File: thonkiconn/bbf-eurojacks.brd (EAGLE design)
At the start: 18.4 x 52.1 mm, 7 parts, among them U1 THONKICONNNEW, U2 THONKICONNNEW, U3 THONKI-STEREO, U4 THONKI-STEREO

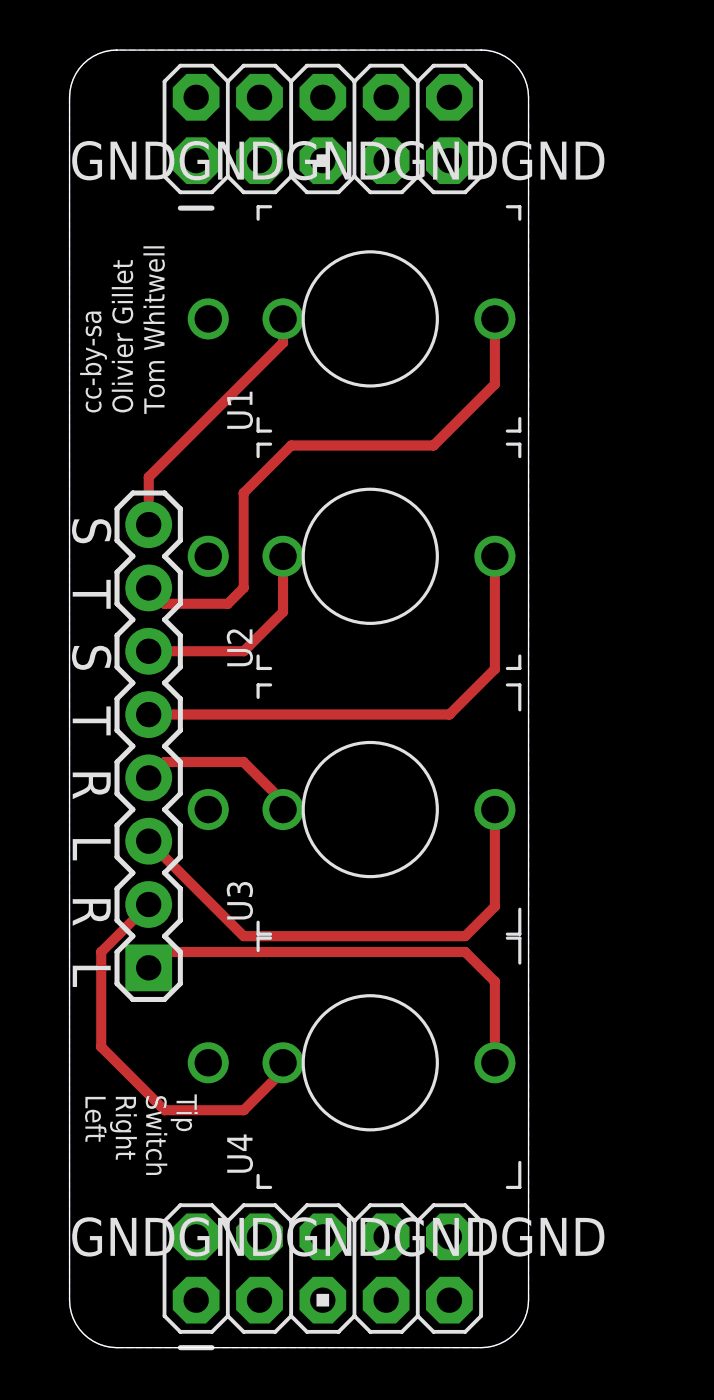
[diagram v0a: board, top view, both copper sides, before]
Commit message: Finished updated eurojacks board
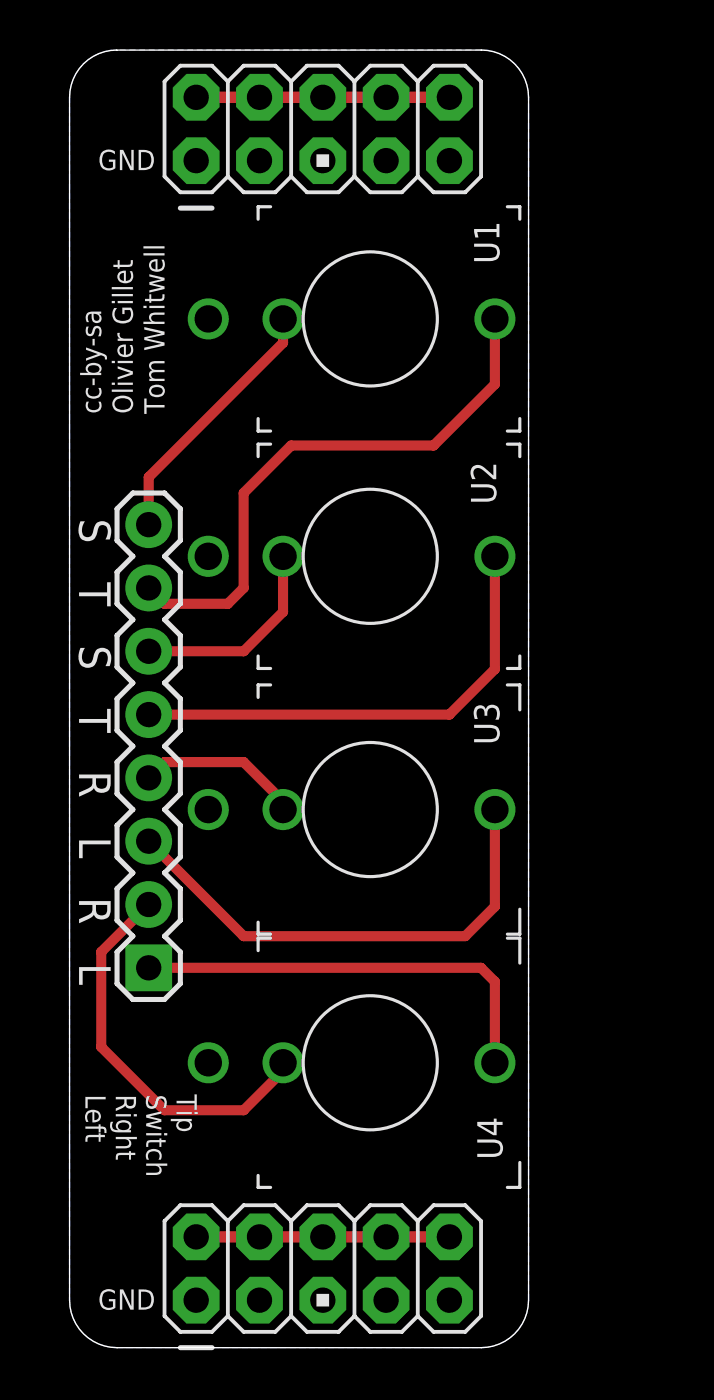
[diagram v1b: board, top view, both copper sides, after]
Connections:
- net GND: now also JP3.1, JP3.3, JP3.5, JP3.7, JP3.9; no longer JP3.10, JP3.2, JP3.4, JP3.6, JP3.8
- net VEE: now also JP3.10, JP3.2, JP3.4, JP3.6, JP3.8; no longer JP3.1, JP3.3, JP3.5, JP3.7, JP3.9
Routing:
- net VEE: track 0.00 -> 10.2 mm
- net VCC: track 0.00 -> 10.2 mm
- net 4-LEFT: track 17.9 -> 17.4 mm
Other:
- board text added: "GND"
- board text removed: "GNDGNDGNDGNDGND"
